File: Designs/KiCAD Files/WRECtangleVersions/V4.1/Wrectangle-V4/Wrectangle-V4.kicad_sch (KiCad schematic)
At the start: 66 parts, among them J10 xBee-Antenna1, J2 USB_C_Receptacle_USB2.0_16P, J3 AnalogIn-Terminal3, J4 AnalogIn-Terminal2, J5 AnalogIn-Terminal1, J6 AnalogIn-Terminal0, J7 GPS-Antenna, J8 Micro_SD_Card, U1 STM32F405RGTx, U10 FT232RL, U11 BME280, U2 BNO085_C5189642, U3 MAX-M10S-00B, U4 H3LIS331DLTR, U9 XBP9X-DMUS-001

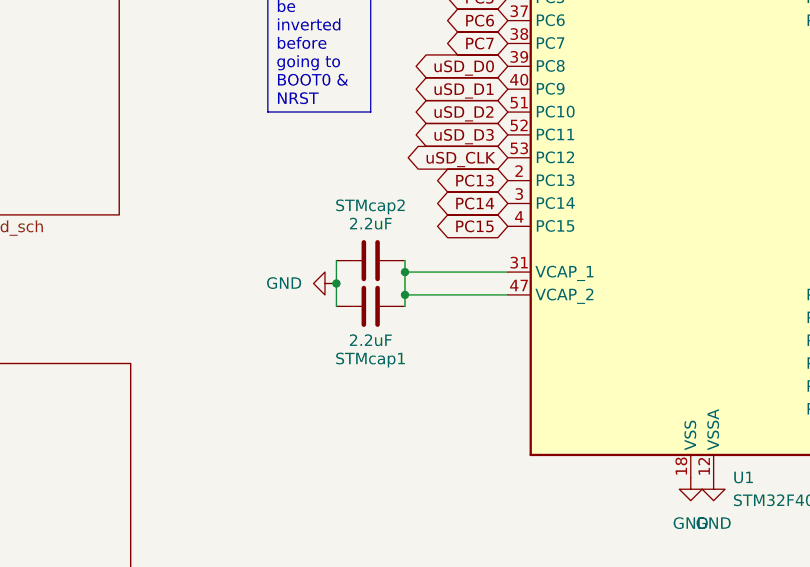
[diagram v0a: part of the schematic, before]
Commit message: Update Wrectangle-V4.kicad_sch
Fixed a wire.
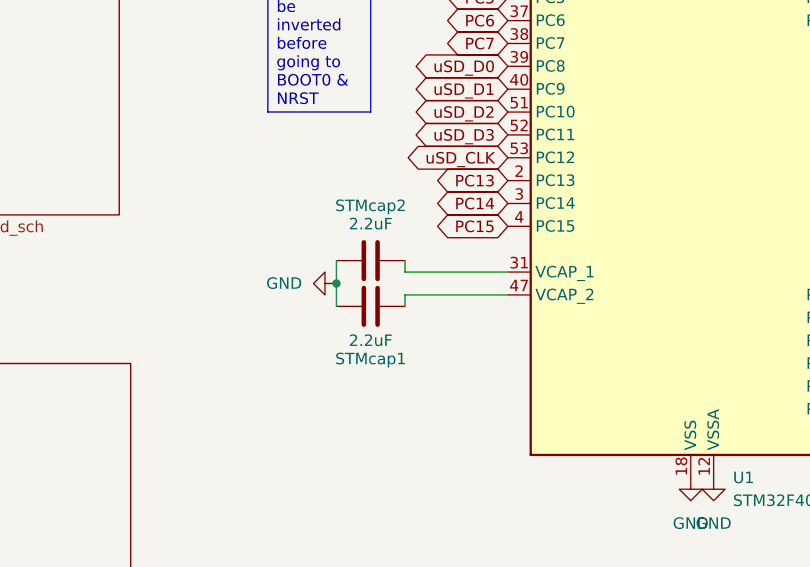
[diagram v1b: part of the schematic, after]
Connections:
- net at STMcap2.2, U1.31 (VCAP_1): no longer STMcap1.2, U1.47 (VCAP_2)
- new net: STMcap1.2, U1.47 (VCAP_2)
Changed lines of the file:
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@@
-	)
-	(junction
-		(at 27.94 102.87)
-		(diameter 0)
-		(color 0 0 0 0)
 	)
 	(junction
@@
 	)
 	(junction
-		(at 27.94 105.41)
-		(diameter 0)
-		(color 0 0 0 0)
-	)
-	(junction
 		(at 114.3 83.82)
 		(diameter 0)
@@
 		)
 		(stroke
-			(width 0)
-			(type default)
-		)
-	)
-	(wire
-		(pts
-			(xy 27.94 102.87) (xy 27.94 105.41)
-		)
-		(stroke
